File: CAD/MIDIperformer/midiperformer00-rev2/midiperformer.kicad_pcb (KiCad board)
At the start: 2 copper layers, 45 x 42 mm, 34 parts, among them J1 MIDI IN B, J2 MIDI IN A, J3 MIDI OUT A, J4 MIDI OUT B, J5 Barrel_Jack, J6 Conn_02x08_Counter_Clockwise, SW1 SW_Push, U1 6N138, U2 6N138, U3 L7805, U4 Teensy-LC, U5 WS2812

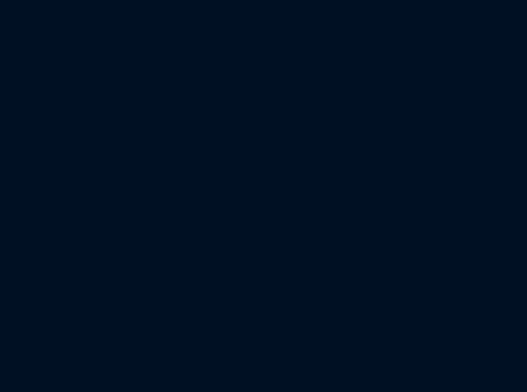
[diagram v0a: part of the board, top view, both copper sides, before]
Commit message: adding a hardware layout sketch to the midi performer device PCB progress on the clarinoid3 body
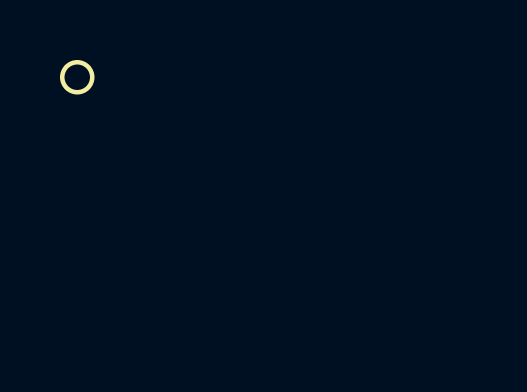
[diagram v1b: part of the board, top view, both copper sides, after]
